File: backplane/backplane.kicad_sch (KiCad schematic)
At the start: 16 parts, among them U101 MCP23008-xSO, U102 PCA9548ADB, U103 AT24CS32-SSHM

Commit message: More backplane work
- Added pull up/down resistors at end of board to bring the various
  data/address lines to a controlled state, rather than floating, and
  attempt to control reflections

- Added a clock buffer so each slot gets its own nice buffered clock.

  The clock buffer used is only 1:5 fanout, so the last two slots share
  a clock line.
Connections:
- net I2C_SDA5: now reaches U102.10 (SD3)
- net I2C_SCL5: now reaches U102.11 (SC3)
- net I2C_SDA0: now reaches U102.13 (SD4)
- net I2C_SCL0: now reaches U102.14 (SC4)
- net I2C_SDA1: now reaches U102.15 (SD5)
- net I2C_SCL1: now reaches U102.16 (SC5)
- net I2C_SDA2: now reaches U102.4 (SD0)
- net I2C_SCL2: now reaches U102.5 (SC0)
- net I2C_SDA3: now reaches U102.6 (SD1)
- net I2C_SCL3: now reaches U102.7 (SC1)
- net I2C_SDA4: now reaches U102.8 (SD2)
- net I2C_SCL4: now reaches U102.9 (SC2)
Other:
- sheet Expansion Slots ports: added CLK; removed none

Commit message: Added audio mixer to backplane
- Implemented mixing (via resistors and an op amp) for the audio outputs
  from each slot and CPU card. These inputs are tied to ground through
  weak pull downs, so peripherals can leave the pins open if they're not
  being used.

  It's possible that the resistance values for the mixer aren't quite
  correct and will produce a distorted mess with many peripherals
  outputting sound simultaneously; if that's an issue, we can adjust the
  value of the resistors or add per slot trimmers to adjust each slots'
  relative volume.
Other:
- added sheet Audio Mixer (Audio.kicad_sch)
- sheet Expansion Slots ports: added SNDL[0..5], SNDR[0..5]; removed none
- note added: "Address: 0b1010111 / 0b1011111"

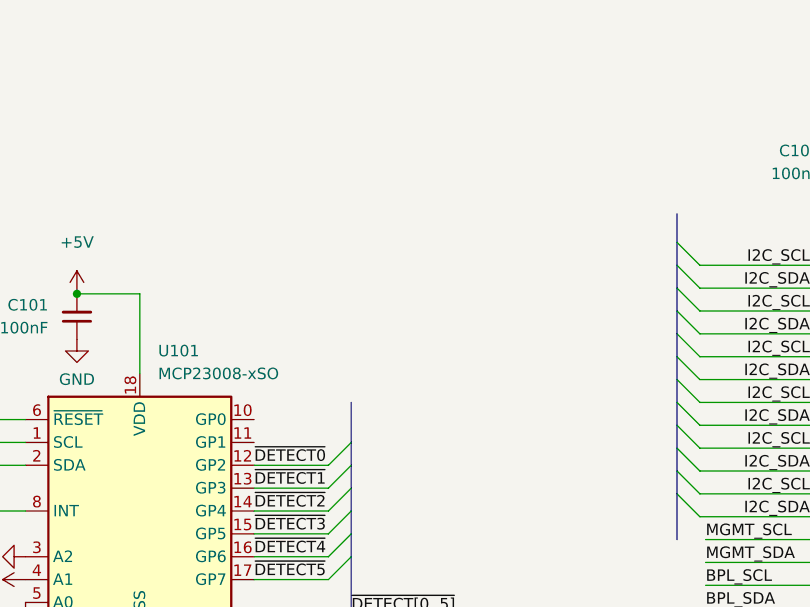
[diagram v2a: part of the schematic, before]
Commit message: More optimization of backplane
- Fixed a few DRC errors and added LEDs with the spare IOs on the I2C
  expander.
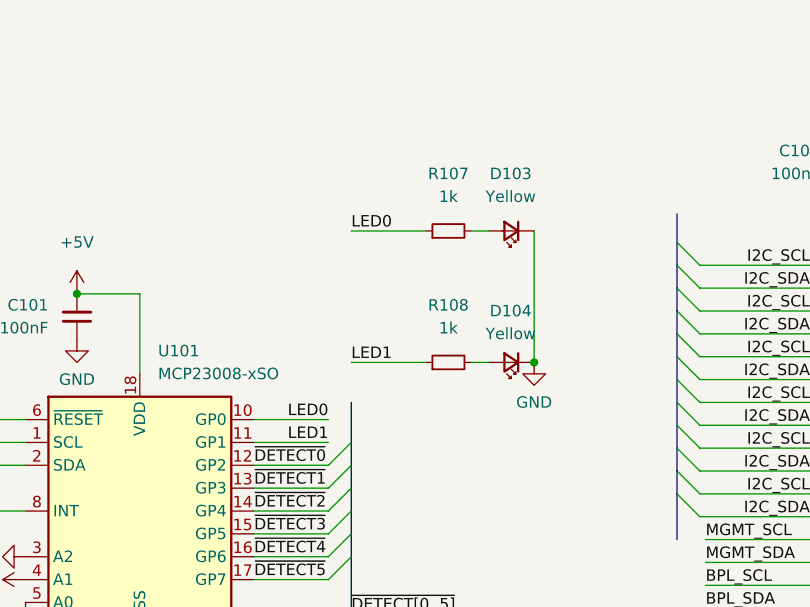
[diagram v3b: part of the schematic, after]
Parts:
- added D103, D104: Yellow, LED_SMD:LED_0805_2012Metric, symbol Device:LED_Small
- added R107, R108: 1k, Resistor_SMD:R_0805_2012Metric, symbol Device:R_Small
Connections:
- net GND: now also D103.1 (K), D104.1 (K)
- net LED0: now reaches U101.10 (GP0)
- net LED0: now also R107.1
- net LED1: now reaches U101.11 (GP1)
- net LED1: now also R108.1
- new net: D104.2 (A), R108.2
- new net: D103.2 (A), R107.2
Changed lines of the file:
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@@
 (kicad_sch (version 20211123) (generator eeschema)
   (paper "A4")
+  (junction (at 93.345 153.67) (diameter 0) (color 0 0 0 0)
+  )
   (junction (at 237.49 146.05) (diameter 0) (color 0 0 0 0)
   )
@@
     (stroke (width 0) (type default) (color 0 0 0 0))
   )
+  (wire (pts (xy 81.28 153.67) (xy 73.025 153.67))
+    (stroke (width 0) (type default) (color 0 0 0 0))
+  )
   (bus (pts (xy 73.025 175.26) (xy 73.025 181.61))
     (stroke (width 0) (type default) (color 0 0 0 0))
@@
     (stroke (width 0) (type default) (color 0 0 0 0))
   )
+  (wire (pts (xy 86.36 153.67) (xy 88.265 153.67))
+    (stroke (width 0) (type default) (color 0 0 0 0))
+  )
   (wire (pts (xy 257.81 143.51) (xy 269.875 143.51))
     (stroke (width 0) (type default) (color 0 0 0 0))
@@
     (stroke (width 0) (type default) (color 0 0 0 0))
   )
+  (wire (pts (xy 73.025 139.065) (xy 81.28 139.065))
+    (stroke (width 0) (type default) (color 0 0 0 0))
+  )
   (wire (pts (xy 40.005 46.99) (xy 52.705 46.99))
     (stroke (width 0) (type default) (color 0 0 0 0))
@@
     (stroke (width 0) (type default) (color 0 0 0 0))
   )
+  (wire (pts (xy 62.23 160.02) (xy 70.485 160.02))
+    (stroke (width 0) (type default) (color 0 0 0 0))
+  )
+  (wire (pts (xy 93.345 139.065) (xy 93.345 153.67))
+    (stroke (width 0) (type default) (color 0 0 0 0))
+  )
+  (wire (pts (xy 62.23 162.56) (xy 70.485 162.56))
+    (stroke (width 0) (type default) (color 0 0 0 0))
+  )
   (wire (pts (xy 40.005 37.465) (xy 52.705 37.465))
     (stroke (width 0) (type default) (color 0 0 0 0))
@@
     (stroke (width 0) (type default) (color 0 0 0 0))
   )
+  (wire (pts (xy 86.36 139.065) (xy 88.265 139.065))
+    (stroke (width 0) (type default) (color 0 0 0 0))
+  )
   (wire (pts (xy 243.84 86.995) (xy 256.54 86.995))
     (stroke (width 0) (type default) (color 0 0 0 0))
@@
     (effects (font (size 1.27 1.27)) (justify left bottom))
   )
+  (label "LED0" (at 73.025 139.065 0)
+    (effects (font (size 1.27 1.27)) (justify left bottom))
+  )
   (label "R{slash}~{W}" (at 52.705 62.23 180)
     (effects (font (size 1.27 1.27)) (justify right bottom))
@@
     (effects (font (size 1.27 1.27)) (justify left bottom))
   )
+  (label "LED1" (at 73.025 153.67 0)
+    (effects (font (size 1.27 1.27)) (justify left bottom))
+  )
   (label "MGMT_SCL" (at 112.395 173.355 0)
     (effects (font (size 1.27 1.27)) (justify left bottom))
@@
     (effects (font (size 1.27 1.27)) (justify left bottom))
   )
+  (label "LED0" (at 70.485 160.02 180)
+    (effects (font (size 1.27 1.27)) (justify right bottom))
+  )
   (label "BPL_SDA" (at 111.76 22.225 180)
+    (effects (font (size 1.27 1.27)) (justify right bottom))
+  )
+  (label "LED1" (at 70.485 162.56 180)
     (effects (font (size 1.27 1.27)) (justify right bottom))
   )
@@
     )
     (pin "1")
+  )
+  (symbol (lib_id "Device:LED_Small") (at 90.805 153.67 180) (unit 1)
+    (in_bom yes) (on_board yes) (fields_autoplaced)
+    (property "Reference" "D104" (id 0) (at 90.7415 147.955 0))
+    (property "Value" "Yellow" (id 1) (at 90.7415 150.495 0))
+    (property "Footprint" "LED_SMD:LED_0805_2012Metric" (id 2) (at 90.805 153.67 90)
+      (effects (font (size 1.27 1.27)) hide)
+    )
+    (property "Datasheet" "~" (id 3) (at 90.805 153.67 90)
+      (effects (font (size 1.27 1.27)) hide)
+    )
+    (property "MPN" "AP2012YD" (id 4) (at 90.805 153.67 0)
+      (effects (font (size 1.27 1.27)) hide)
+    )
+    (pin "1")
+    (pin "2")
   )
   (symbol (lib_id "power:GND") (at 42.545 151.13 0) (unit 1)
@@
     (pin "2")
   )
+  (symbol (lib_id "Device:R_Small") (at 83.82 139.065 90) (unit 1)
+    (in_bom yes) (on_board yes) (fields_autoplaced)
+    (property "Reference" "R107" (id 0) (at 83.82 132.715 90))
+    (property "Value" "1k" (id 1) (at 83.82 135.255 90))
+    (property "Footprint" "Resistor_SMD:R_0805_2012Metric" (id 2) (at 83.82 139.065 0)
+      (effects (font (size 1.27 1.27)) hide)
+    )
+    (property "Datasheet" "~" (id 3) (at 83.82 139.065 0)
+      (effects (font (size 1.27 1.27)) hide)
+    )
+    (pin "1")
+    (pin "2")
+  )
   (symbol (lib_id "Jumper:Jumper_3_Bridged12") (at 276.86 148.59 270) (mirror x) (unit 1)
     (in_bom yes) (on_board yes) (fields_autoplaced)
@@
     (pin "1")
   )
+  (symbol (lib_id "Device:LED_Small") (at 90.805 139.065 180) (unit 1)
+    (in_bom yes) (on_board yes) (fields_autoplaced)
+    (property "Reference" "D103" (id 0) (at 90.7415 132.715 0))
+    (property "Value" "Yellow" (id 1) (at 90.7415 135.255 0))
+    (property "Footprint" "LED_SMD:LED_0805_2012Metric" (id 2) (at 90.805 139.065 90)
+      (effects (font (size 1.27 1.27)) hide)
+    )
+    (property "Datasheet" "~" (id 3) (at 90.805 139.065 90)
+      (effects (font (size 1.27 1.27)) hide)
+    )
+    (property "MPN" "AP2012YD" (id 4) (at 90.805 139.065 0)
+      (effects (font (size 1.27 1.27)) hide)
+    )
+    (pin "1")
+    (pin "2")
+  )
   (symbol (lib_id "power:GND") (at 247.65 153.67 0) (unit 1)
     (in_bom yes) (on_board yes) (fields_autoplaced)
@@
     )
     (property "Datasheet" "" (id 3) (at 247.65 153.67 0)
+      (effects (font (size 1.27 1.27)) hide)
+    )
+    (pin "1")
+  )
+  (symbol (lib_id "Device:R_Small") (at 83.82 153.67 90) (unit 1)
+    (in_bom yes) (on_board yes) (fields_autoplaced)
+    (property "Reference" "R108" (id 0) (at 83.82 147.32 90))
+    (property "Value" "1k" (id 1) (at 83.82 149.86 90))
+    (property "Footprint" "Resistor_SMD:R_0805_2012Metric" (id 2) (at 83.82 153.67 0)
+      (effects (font (size 1.27 1.27)) hide)
+    )
+    (property "Datasheet" "~" (id 3) (at 83.82 153.67 0)
+      (effects (font (size 1.27 1.27)) hide)
+    )
+    (pin "1")
+    (pin "2")
+  )
+  (symbol (lib_id "power:GND") (at 93.345 153.67 0) (unit 1)
+    (in_bom yes) (on_board yes) (fields_autoplaced)
+    (property "Reference" "#PWR0129" (id 0) (at 93.345 160.02 0)
+      (effects (font (size 1.27 1.27)) hide)
+    )
+    (property "Value" "GND" (id 1) (at 93.345 158.115 0))
+    (property "Footprint" "" (id 2) (at 93.345 153.67 0)
+      (effects (font (size 1.27 1.27)) hide)
+    )
+    (property "Datasheet" "" (id 3) (at 93.345 153.67 0)
       (effects (font (size 1.27 1.27)) hide)
     )
@@
       (reference "#PWR0128") (unit 1) (value "+5V") (footprint "")
     )
+    (path "/ae0d4b72-4047-405d-9263-4f30f04ae4df"
+      (reference "#PWR0129") (unit 1) (value "GND") (footprint "")
+    )
     (path "/04faa6f8-09d5-4a29-a760-46b6402b50f3/0d46a8ed-ec03-4364-bd30-b17846a842aa"
       (reference "#PWR0201") (unit 1) (value "+12V") (footprint "")
@@
       (reference "D102") (unit 1) (value "Green") (footprint "LED_SMD:LED_0805_2012Metric")
     )
+    (path "/9dd4dac1-404e-44d1-8a21-1a22afcdec32"
+      (reference "D103") (unit 1) (value "Yellow") (footprint "LED_SMD:LED_0805_2012Metric")
+    )
+    (path "/33f617d6-3ffc-4902-8dfa-2e8bb0fa4071"
+      (reference "D104") (unit 1) (value "Yellow") (footprint "LED_SMD:LED_0805_2012Metric")
+    )
     (path "/04faa6f8-09d5-4a29-a760-46b6402b50f3/be4c08f8-5be7-4a72-971d-68a412b6beb2"
       (reference "J201") (unit 1) (value "Management") (footprint "Connector_DIN:DIN41612_C2_3x16_Female_Vertical_THT")
@@
       (reference "R106") (unit 1) (value "4k7") (footprint "Resistor_SMD:R_0805_2012Metric")
     )
+    (path "/7cbd23f9-3610-4264-860b-52bca94b4075"
+      (reference "R107") (unit 1) (value "1k") (footprint "Resistor_SMD:R_0805_2012Metric")
+    )
+    (path "/a3af4acc-00b1-4aa5-bdde-9dc62d87ee81"
+      (reference "R108") (unit 1) (value "1k") (footprint "Resistor_SMD:R_0805_2012Metric")
+    )
     (path "/68db9397-0a5f-44ed-adc6-f2d20a7e80bf/380e2174-dc94-47bf-8ff6-612d43eee02b"

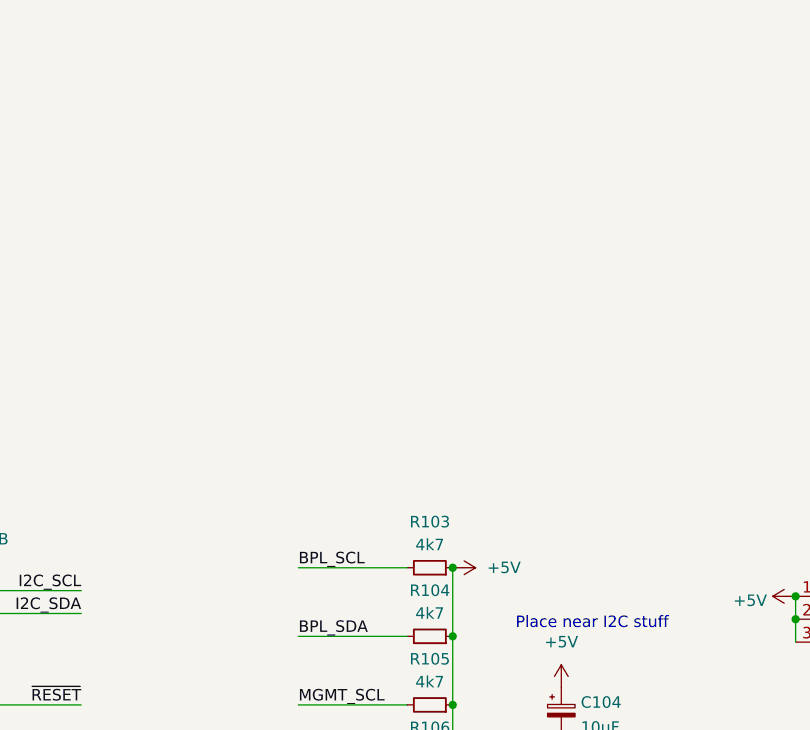
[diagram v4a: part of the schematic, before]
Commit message: Added missing screw holes to backplane
- These apparently got removed at some point before the commit that said
  they were added got made, likely when updating the board from
  schematic. They were added back, though the X positioning may not be
  quite correct.
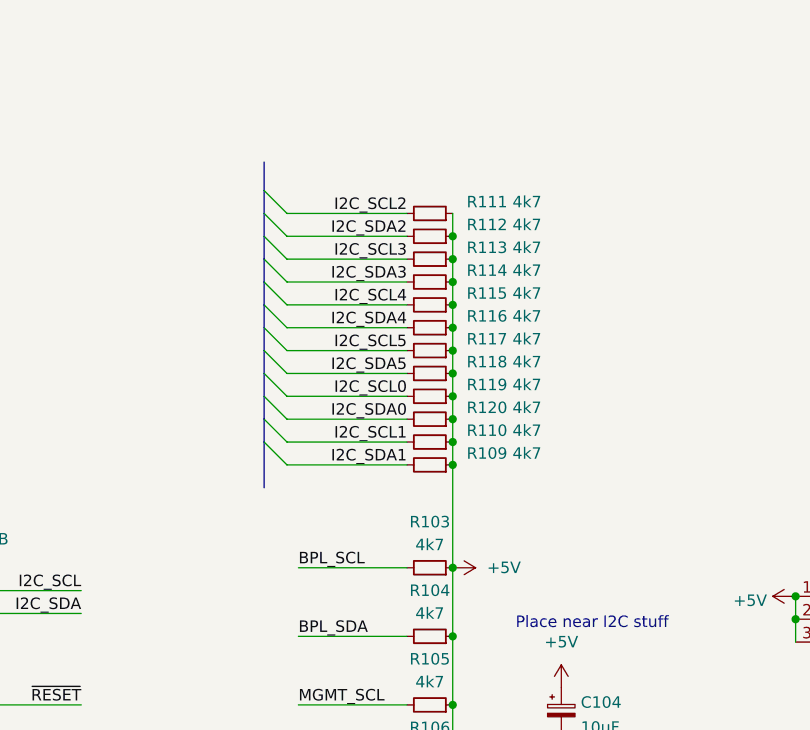
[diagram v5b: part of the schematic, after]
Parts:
- added R109, R110, R111, R112, R113, R114, R115, R116, R117, R118, R119, R120: 4k7, Resistor_SMD:R_0805_2012Metric, symbol Device:R_Small
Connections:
- net +5V: now also R109.1, R110.1, R111.1, R112.1, R113.1, R114.1, R115.1, R116.1, R117.1, R118.1, R119.1, R120.1
- net I2C_SCL0: now also R119.2
- net I2C_SCL1: now also R110.2
- net I2C_SCL2: now also R111.2
- net I2C_SCL3: now also R113.2
- net I2C_SCL4: now also R115.2
- net I2C_SCL5: now also R117.2
- net I2C_SDA0: now also R120.2
- net I2C_SDA1: now also R109.2
- net I2C_SDA2: now also R112.2
- net I2C_SDA3: now also R114.2
- net I2C_SDA4: now also R116.2
- net I2C_SDA5: now also R118.2

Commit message: Minor tweaks to all boards
- Moved around some traces on the 68000 CPU card for prettiness

- Added a connector on the backplane to provide +5V/+12V without a
  management card installed (for testing)
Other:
- company: (none) -> Tristan Seifert
- title: (none) -> Backplane
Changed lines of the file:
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@@
 (kicad_sch (version 20211123) (generator eeschema)
   (paper "A4")
+  (title_block
+    (title "Backplane")
+    (date "2022-01-09")
+    (rev "1")
+    (company "Tristan Seifert")
+  )
   (junction (at 93.345 153.67) (diameter 0) (color 0 0 0 0)
   )
@@
       (reference "#PWR0130") (unit 1) (value "GND") (footprint "")
     )
+    (path "/04faa6f8-09d5-4a29-a760-46b6402b50f3/40f51846-c0b8-42af-9ac0-ed1a062a6b9c"
+      (reference "#PWR0131") (unit 1) (value "+5V") (footprint "")
+    )
+    (path "/04faa6f8-09d5-4a29-a760-46b6402b50f3/1da9b01b-2c1a-4f96-8861-c0ae2f75a1f2"
+      (reference "#PWR0132") (unit 1) (value "GND") (footprint "")
+    )
+    (path "/04faa6f8-09d5-4a29-a760-46b6402b50f3/3743903e-c880-4012-8328-ee9a0832f40a"
+      (reference "#PWR0133") (unit 1) (value "+12V") (footprint "")
+    )
     (path "/04faa6f8-09d5-4a29-a760-46b6402b50f3/0d46a8ed-ec03-4364-bd30-b17846a842aa"
       (reference "#PWR0201") (unit 1) (value "+12V") (footprint "")
@@
       (reference "J201") (unit 2) (value "Management") (footprint "Connector_DIN:DIN41612_C2_3x16_Female_Vertical_THT")
     )
+    (path "/04faa6f8-09d5-4a29-a760-46b6402b50f3/380bbbf0-086b-4e42-86c8-525f89493382"
+      (reference "J202") (unit 1) (value "Screw_Terminal_01x03") (footprint "Connector_Phoenix_MC:PhoenixContact_MCV_1,5_3-GF-3.5_1x03_P3.50mm_Vertical_ThreadedFlange_MountHole")
+    )
     (path "/a24aed28-441e-4b9b-b001-9cc182d3d62b/7eb75285-9dee-41bb-8ef3-814f9a5fc220"

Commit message: Tweaks to bill of materials
- Added missing MPN's for a few components; tweaked a few bits of layout
  to increase some tolerances

  This includes kind of tweaking the boot rom socket positions in hopes
  of fitting fancier sockets
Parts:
- JP101: now left out of the parts list
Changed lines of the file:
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@@
   )
   (symbol (lib_id "Jumper:Jumper_3_Bridged12") (at 276.86 148.59 270) (mirror x) (unit 1)
-    (in_bom yes) (on_board yes) (fields_autoplaced)
+    (in_bom no) (on_board yes) (fields_autoplaced)
     (property "Reference" "JP101" (id 0) (at 278.511 147.6815 90)
       (effects (font (size 1.27 1.27)) (justify left))
